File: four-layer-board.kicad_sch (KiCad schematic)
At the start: 14 parts, among them Q1 AO3401A, U2 AMS1117-3.3

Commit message: Modified gitignore
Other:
- sheet Motor Driver ports: added M2_ENCA, M2_ENCB, M2_IN1, M2_IN2; removed none
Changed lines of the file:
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@@
+      (effects (font (size 1.27 1.27)) (justify right))
+    )
+    (pin "M2_IN2" input (at 93.98 99.06 0)
+      (effects (font (size 1.27 1.27)) (justify right))
+    )
+    (pin "M2_IN1" input (at 93.98 96.52 0)
+      (effects (font (size 1.27 1.27)) (justify right))
+    )
+    (pin "M2_ENCA" output (at 93.98 101.6 0)
+      (effects (font (size 1.27 1.27)) (justify right))
+    )
+    (pin "M2_ENCB" output (at 93.98 104.14 0)
       (effects (font (size 1.27 1.27)) (justify right))
     )
@@
     )
     (path "/38301e58-d617-4386-91a0-b5d6884075ca/fa642142-0abe-4308-a4f1-04c7bda05e7b"
-      (reference "C2") (unit 1) (value "4u7") (footprint "Capacitor_SMD:C_0402_1005Metric")
+      (reference "C2") (unit 1) (value "0u1") (footprint "Capacitor_SMD:C_0402_1005Metric")
     )
     (path "/38301e58-d617-4386-91a0-b5d6884075ca/00eba481-86d5-441c-b57c-f6494f3e419b"

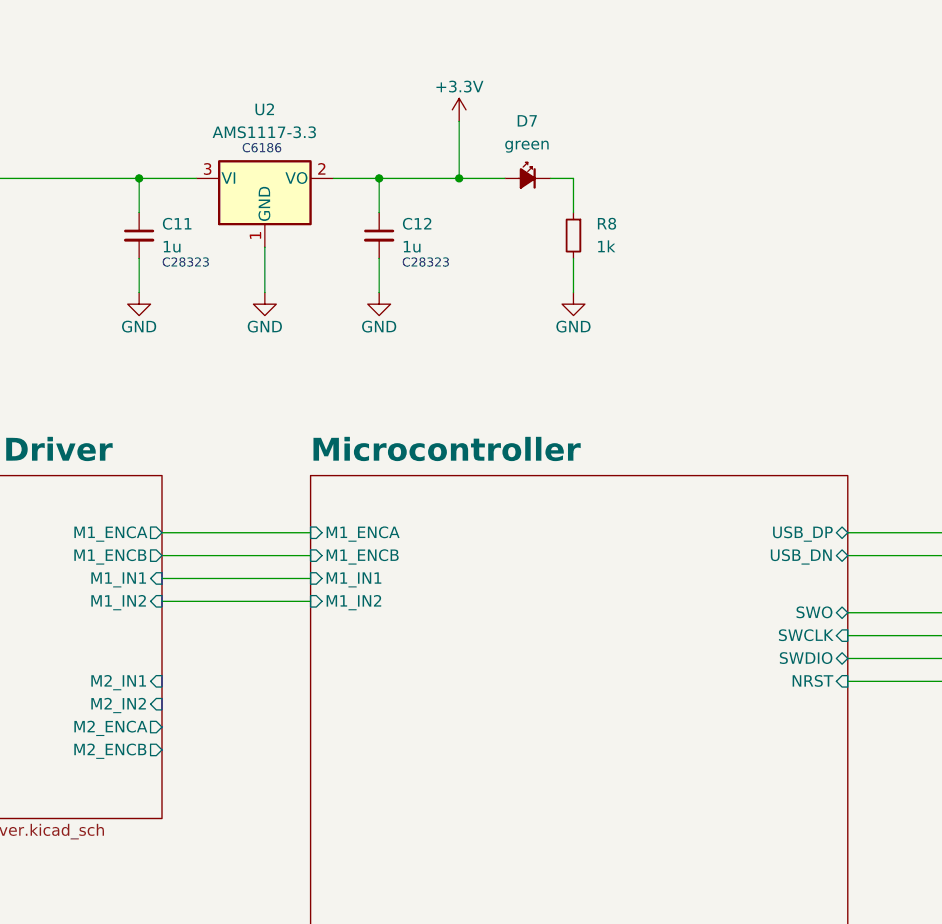
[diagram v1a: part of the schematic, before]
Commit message: Added connections for motor 2
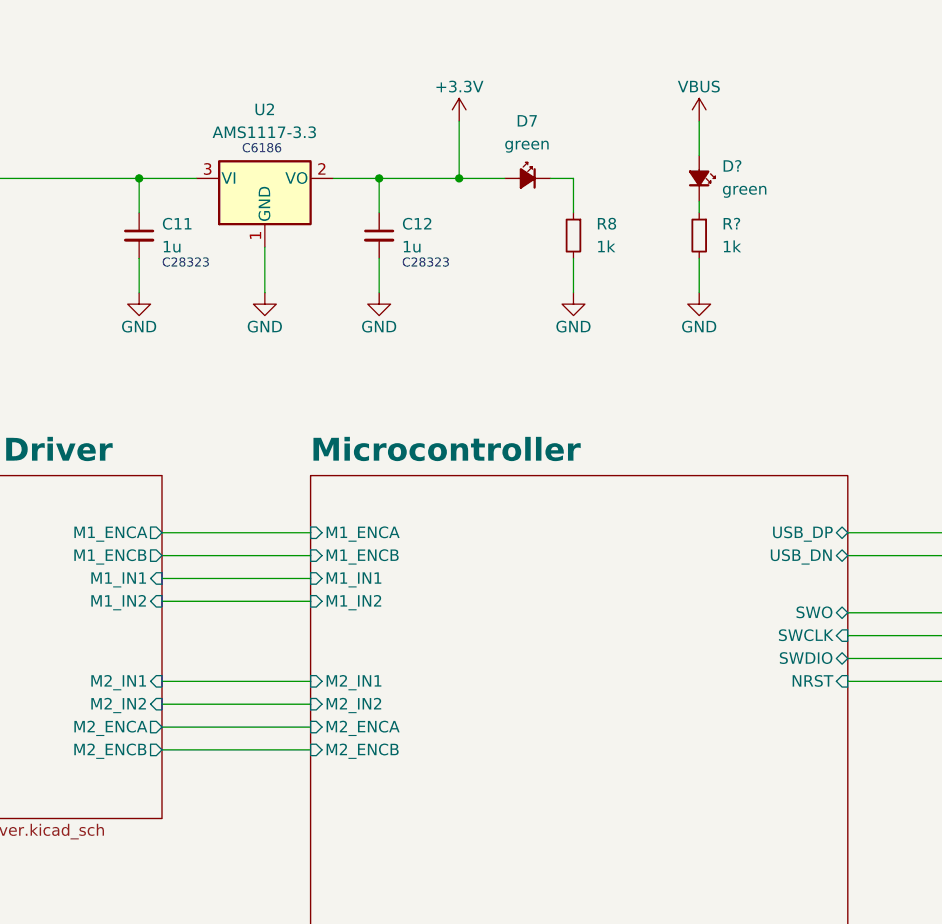
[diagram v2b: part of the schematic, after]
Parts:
- added D?: green, LED_SMD:LED_0603_1608Metric, symbol Device:LED_Small_Filled
- added R?: 1k, Resistor_SMD:R_0603_1608Metric, symbol Device:R_Small
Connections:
- net GND: now also R?.2
- net VBUS: now also D?.2 (A)
- new net: D?.1 (K), R?.1
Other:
- sheet Microcontroller ports: added M2_ENCA, M2_ENCB, M2_IN1, M2_IN2; removed none
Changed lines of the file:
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@@
+    (stroke (width 0) (type default) (color 0 0 0 0))
+  )
+  (wire (pts (xy 153.67 34.29) (xy 153.67 38.1))
     (stroke (width 0) (type default) (color 0 0 0 0))
   )
@@
     (stroke (width 0) (type default) (color 0 0 0 0))
   )
+  (wire (pts (xy 93.98 99.06) (xy 110.49 99.06))
+    (stroke (width 0) (type default) (color 0 0 0 0))
+  )
   (wire (pts (xy 170.18 91.44) (xy 182.88 91.44))
     (stroke (width 0) (type default) (color 0 0 0 0))
   )
+  (wire (pts (xy 153.67 43.18) (xy 153.67 44.45))
+    (stroke (width 0) (type default) (color 0 0 0 0))
+  )
   (wire (pts (xy 71.12 38.1) (xy 71.12 40.64))
     (stroke (width 0) (type default) (color 0 0 0 0))
@@
     (stroke (width 0) (type default) (color 0 0 0 0))
   )
+  (wire (pts (xy 153.67 49.53) (xy 153.67 53.34))
+    (stroke (width 0) (type default) (color 0 0 0 0))
+  )
   (wire (pts (xy 93.98 82.55) (xy 110.49 82.55))
     (stroke (width 0) (type default) (color 0 0 0 0))
@@
     (stroke (width 0) (type default) (color 0 0 0 0))
   )
+  (wire (pts (xy 93.98 101.6) (xy 110.49 101.6))
+    (stroke (width 0) (type default) (color 0 0 0 0))
+  )
   (wire (pts (xy 59.69 48.26) (xy 59.69 53.34))
     (stroke (width 0) (type default) (color 0 0 0 0))
@@
     (stroke (width 0) (type default) (color 0 0 0 0))
   )
+  (wire (pts (xy 93.98 96.52) (xy 110.49 96.52))
+    (stroke (width 0) (type default) (color 0 0 0 0))
+  )
   (wire (pts (xy 170.18 80.01) (xy 182.88 80.01))
     (stroke (width 0) (type default) (color 0 0 0 0))
@@
   )
   (wire (pts (xy 139.7 40.64) (xy 137.16 40.64))
+    (stroke (width 0) (type default) (color 0 0 0 0))
+  )
+  (wire (pts (xy 93.98 104.14) (xy 110.49 104.14))
     (stroke (width 0) (type default) (color 0 0 0 0))
   )
@@
     )
   )
+  (symbol (lib_id "power:VBUS") (at 153.67 34.29 0) (unit 1)
+    (in_bom yes) (on_board yes)
+    (property "Reference" "#PWR?" (id 0) (at 153.67 38.1 0)
+      (effects (font (size 1.27 1.27)) hide)
+    )
+    (property "Value" "VBUS" (id 1) (at 153.67 30.48 0))
+    (property "Footprint" "" (id 2) (at 153.67 34.29 0)
+      (effects (font (size 1.27 1.27)) hide)
+    )
+    (property "Datasheet" "" (id 3) (at 153.67 34.29 0)
+      (effects (font (size 1.27 1.27)) hide)
+    )
+    (pin "1")
+  )
   (symbol (lib_id "Device:LED_Small_Filled") (at 36.83 40.64 0) (unit 1)
     (in_bom yes) (on_board yes) (fields_autoplaced)
@@
     (pin "3")
   )
+  (symbol (lib_id "Device:LED_Small_Filled") (at 153.67 40.64 270) (mirror x) (unit 1)
+    (in_bom yes) (on_board yes) (fields_autoplaced)
+    (property "Reference" "D?" (id 0) (at 156.21 39.3064 90)
+      (effects (font (size 1.27 1.27)) (justify left))
+    )
+    (property "Value" "green" (id 1) (at 156.21 41.8464 90)
+      (effects (font (size 1.27 1.27)) (justify left))
+    )
+    (property "Footprint" "LED_SMD:LED_0603_1608Metric" (id 2) (at 153.67 40.64 90)
+      (effects (font (size 1.27 1.27)) hide)
+    )
+    (property "Datasheet" "~" (id 3) (at 153.67 40.64 90)
+      (effects (font (size 1.27 1.27)) hide)
+    )
+    (pin "1")
+    (pin "2")
+  )
   (symbol (lib_id "power:GND") (at 118.11 53.34 0) (unit 1)
     (in_bom yes) (on_board yes)
@@
     )
     (pin "1")
+  )
+  (symbol (lib_id "power:GND") (at 153.67 53.34 0) (mirror y) (unit 1)
+    (in_bom yes) (on_board yes)
+    (property "Reference" "#PWR?" (id 0) (at 153.67 59.69 0)
+      (effects (font (size 1.27 1.27)) hide)
+    )
+    (property "Value" "GND" (id 1) (at 153.67 57.15 0))
+    (property "Footprint" "" (id 2) (at 153.67 53.34 0)
+      (effects (font (size 1.27 1.27)) hide)
+    )
+    (property "Datasheet" "" (id 3) (at 153.67 53.34 0)
+      (effects (font (size 1.27 1.27)) hide)
+    )
+    (pin "1")
+  )
+  (symbol (lib_id "Device:R_Small") (at 153.67 46.99 0) (mirror y) (unit 1)
+    (in_bom yes) (on_board yes) (fields_autoplaced)
+    (property "Reference" "R?" (id 0) (at 156.21 45.7199 0)
+      (effects (font (size 1.27 1.27)) (justify right))
+    )
+    (property "Value" "1k" (id 1) (at 156.21 48.2599 0)
+      (effects (font (size 1.27 1.27)) (justify right))
+    )
+    (property "Footprint" "Resistor_SMD:R_0603_1608Metric" (id 2) (at 153.67 46.99 0)
+      (effects (font (size 1.27 1.27)) hide)
+    )
+    (property "Datasheet" "~" (id 3) (at 153.67 46.99 0)
+      (effects (font (size 1.27 1.27)) hide)
+    )
+    (pin "1")
+    (pin "2")
   )
   (symbol (lib_id "Device:C_Small") (at 91.44 46.99 0) (unit 1)
@@
       (effects (font (size 1.27 1.27)) (justify left))
     )
+    (pin "M2_IN1" input (at 110.49 96.52 180)
+      (effects (font (size 1.27 1.27)) (justify left))
+    )
+    (pin "M2_ENCA" input (at 110.49 101.6 180)
+      (effects (font (size 1.27 1.27)) (justify left))
+    )
+    (pin "M2_ENCB" input (at 110.49 104.14 180)
+      (effects (font (size 1.27 1.27)) (justify left))
+    )
+    (pin "M2_IN2" input (at 110.49 99.06 180)
+      (effects (font (size 1.27 1.27)) (justify left))
+    )
   )
   (sheet (at 63.5 73.66) (size 30.48 38.1) (fields_autoplaced)
@@
       (reference "#PWR052") (unit 1) (value "GND") (footprint "")
     )
+    (path "/2f2dc9ef-7e1b-45af-b150-2e2af3cc9f5f"
+      (reference "#PWR?") (unit 1) (value "VBUS") (footprint "")
+    )
+    (path "/a1916798-bb9e-4ca1-9024-e5bc73efde26"
+      (reference "#PWR?") (unit 1) (value "GND") (footprint "")
+    )
     (path "/38301e58-d617-4386-91a0-b5d6884075ca/fb13da7d-92f8-4904-b335-575c2803864e"
       (reference "C1") (unit 1) (value "20p") (footprint "Capacitor_SMD:C_0402_1005Metric")
@@
       (reference "D11") (unit 1) (value "LL4148") (footprint "Diode_SMD:D_MiniMELF")
     )
+    (path "/6653dcad-47c5-4d12-9b6f-4cb4de2a2f3a"
+      (reference "D?") (unit 1) (value "green") (footprint "LED_SMD:LED_0603_1608Metric")
+    )
     (path "/d3e10d87-59ed-4cd4-9f32-e9aa8deb81a2"
       (reference "H1") (unit 1) (value "M3") (footprint "MountingHole:MountingHole_3.2mm_M3_DIN965_Pad")
@@
       (reference "R12") (unit 1) (value "1k5") (footprint "Resistor_SMD:R_0603_1608Metric")
     )
+    (path "/a6371022-78a3-422e-a97f-9e1eb0740b46"
+      (reference "R?") (unit 1) (value "1k") (footprint "Resistor_SMD:R_0603_1608Metric")
+    )
     (path "/38301e58-d617-4386-91a0-b5d6884075ca/2d758403-d18d-4f70-9945-02135508fd40"
